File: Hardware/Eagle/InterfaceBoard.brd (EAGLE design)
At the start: 20 parts

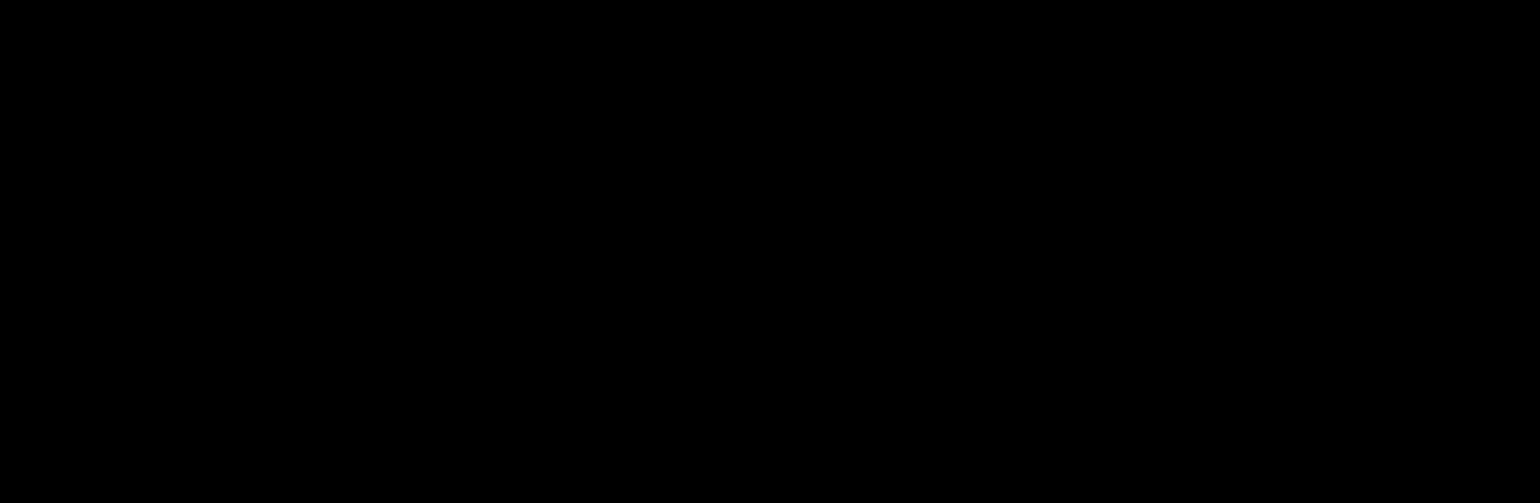
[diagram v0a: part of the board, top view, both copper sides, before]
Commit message: Specified button colors and added Designed by in the PCB layout
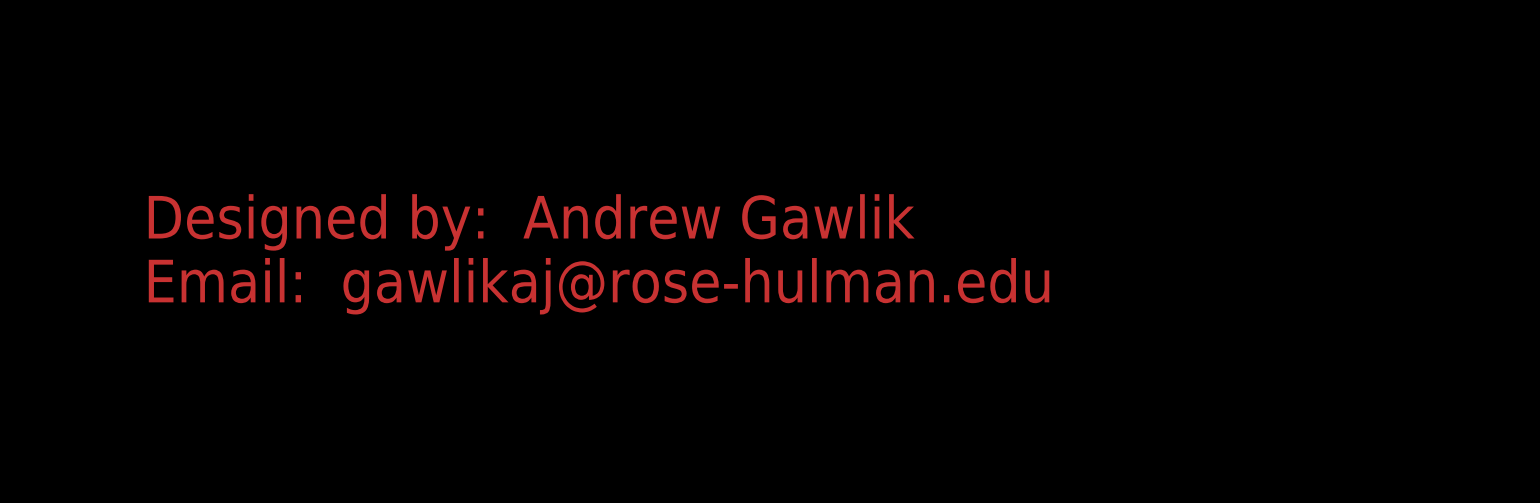
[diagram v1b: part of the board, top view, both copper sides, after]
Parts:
- B0, B9: value (none) -> GREEN
- B1, B6: value (none) -> RED
- B2, B7: value (none) -> BLUE
- B3, B8: value (none) -> YELLOW
- B4, B5: value (none) -> BLACK
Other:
- board text added: "Designed by: Andrew Gawlik Email: gawlikaj@rose-hulman.edu"
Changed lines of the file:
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@@
 <board>
 <plain>
+<text x="88.9" y="-10.16" size="1.778" layer="1">Designed by:  Andrew Gawlik
+Email:  gawlikaj@rose-hulman.edu</text>
 </plain>
 <attributes>
@@
 </autorouter>
 <elements>
-<element name="B9" library="switch-omron" library_urn="urn:adsk.eagle:library:377" package="B3F-10XX" package3d_urn="urn:adsk.eagle:package:27496/1" value="" x="13.335" y="46.99" smashed="yes" rot="R90">
+<element name="B9" library="switch-omron" library_urn="urn:adsk.eagle:library:377" package="B3F-10XX" package3d_urn="urn:adsk.eagle:package:27496/1" value="GREEN" x="13.335" y="46.99" smashed="yes" rot="R90">
 <attribute name="MF" value="" x="13.335" y="46.99" size="1.778" layer="27" rot="R90" display="off"/>
 <attribute name="MPN" value="B3F-1000" x="13.335" y="46.99" size="1.778" layer="27" rot="R90" display="off"/>
@@
 <attribute name="VALUE" x="18.415" y="43.942" size="1.27" layer="27" ratio="10" rot="R90"/>
 </element>
-<element name="B6" library="switch-omron" library_urn="urn:adsk.eagle:library:377" package="B3F-10XX" package3d_urn="urn:adsk.eagle:package:27496/1" value="" x="24.13" y="35.56" smashed="yes" rot="R90">
+<element name="B6" library="switch-omron" library_urn="urn:adsk.eagle:library:377" package="B3F-10XX" package3d_urn="urn:adsk.eagle:package:27496/1" value="RED" x="24.13" y="35.56" smashed="yes" rot="R90">
 <attribute name="MF" value="" x="24.13" y="35.56" size="1.778" layer="27" rot="R90" display="off"/>
 <attribute name="MPN" value="B3F-1000" x="24.13" y="35.56" size="1.778" layer="27" rot="R90" display="off"/>
@@
 <attribute name="VALUE" x="29.21" y="32.512" size="1.27" layer="27" ratio="10" rot="R90"/>
 </element>
-<element name="B7" library="switch-omron" library_urn="urn:adsk.eagle:library:377" package="B3F-10XX" package3d_urn="urn:adsk.eagle:package:27496/1" value="" x="13.335" y="25.4" smashed="yes" rot="R90">
+<element name="B7" library="switch-omron" library_urn="urn:adsk.eagle:library:377" package="B3F-10XX" package3d_urn="urn:adsk.eagle:package:27496/1" value="BLUE" x="13.335" y="25.4" smashed="yes" rot="R90">
 <attribute name="MF" value="" x="13.335" y="25.4" size="1.778" layer="27" rot="R90" display="off"/>
 <attribute name="MPN" value="B3F-1000" x="13.335" y="25.4" size="1.778" layer="27" rot="R90" display="off"/>
@@
 <attribute name="VALUE" x="18.415" y="22.352" size="1.27" layer="27" ratio="10" rot="R90"/>
 </element>
-<element name="B8" library="switch-omron" library_urn="urn:adsk.eagle:library:377" package="B3F-10XX" package3d_urn="urn:adsk.eagle:package:27496/1" value="" x="2.54" y="35.56" smashed="yes" rot="R90">
+<element name="B8" library="switch-omron" library_urn="urn:adsk.eagle:library:377" package="B3F-10XX" package3d_urn="urn:adsk.eagle:package:27496/1" value="YELLOW" x="2.54" y="35.56" smashed="yes" rot="R90">
 <attribute name="MF" value="" x="2.54" y="35.56" size="1.778" layer="27" rot="R90" display="off"/>
 <attribute name="MPN" value="B3F-1000" x="2.54" y="35.56" size="1.778" layer="27" rot="R90" display="off"/>
@@
 <attribute name="VALUE" x="38.9636" y="51.8414" size="0.9906" layer="27" ratio="10" rot="R180"/>
 </element>
-<element name="B2" library="switch-omron" library_urn="urn:adsk.eagle:library:377" package="B3F-10XX" package3d_urn="urn:adsk.eagle:package:27496/1" value="" x="127.635" y="25.4" smashed="yes" rot="R270">
+<element name="B2" library="switch-omron" library_urn="urn:adsk.eagle:library:377" package="B3F-10XX" package3d_urn="urn:adsk.eagle:package:27496/1" value="BLUE" x="127.635" y="25.4" smashed="yes" rot="R270">
 <attribute name="MF" value="" x="127.635" y="25.4" size="1.778" layer="27" rot="R270" display="off"/>
 <attribute name="MPN" value="B3F-1000" x="127.635" y="25.4" size="1.778" layer="27" rot="R270" display="off"/>
@@
 <attribute name="VALUE" x="122.555" y="28.448" size="1.27" layer="27" ratio="10" rot="R270"/>
 </element>
-<element name="B3" library="switch-omron" library_urn="urn:adsk.eagle:library:377" package="B3F-10XX" package3d_urn="urn:adsk.eagle:package:27496/1" value="" x="116.84" y="35.56" smashed="yes" rot="R270">
+<element name="B3" library="switch-omron" library_urn="urn:adsk.eagle:library:377" package="B3F-10XX" package3d_urn="urn:adsk.eagle:package:27496/1" value="YELLOW" x="116.84" y="35.56" smashed="yes" rot="R270">
 <attribute name="MF" value="" x="116.84" y="35.56" size="1.778" layer="27" rot="R270" display="off"/>
 <attribute name="MPN" value="B3F-1000" x="116.84" y="35.56" size="1.778" layer="27" rot="R270" display="off"/>
@@
 <attribute name="VALUE" x="111.76" y="38.608" size="1.27" layer="27" ratio="10" rot="R270"/>
 </element>
-<element name="B0" library="switch-omron" library_urn="urn:adsk.eagle:library:377" package="B3F-10XX" package3d_urn="urn:adsk.eagle:package:27496/1" value="" x="127.635" y="46.99" smashed="yes" rot="R270">
+<element name="B0" library="switch-omron" library_urn="urn:adsk.eagle:library:377" package="B3F-10XX" package3d_urn="urn:adsk.eagle:package:27496/1" value="GREEN" x="127.635" y="46.99" smashed="yes" rot="R270">
 <attribute name="MF" value="" x="127.635" y="46.99" size="1.778" layer="27" rot="R270" display="off"/>
 <attribute name="MPN" value="B3F-1000" x="127.635" y="46.99" size="1.778" layer="27" rot="R270" display="off"/>
@@
 <attribute name="VALUE" x="122.555" y="50.038" size="1.27" layer="27" ratio="10" rot="R270"/>
 </element>
-<element name="B1" library="switch-omron" library_urn="urn:adsk.eagle:library:377" package="B3F-10XX" package3d_urn="urn:adsk.eagle:package:27496/1" value="" x="138.43" y="35.56" smashed="yes" rot="R270">
+<element name="B1" library="switch-omron" library_urn="urn:adsk.eagle:library:377" package="B3F-10XX" package3d_urn="urn:adsk.eagle:package:27496/1" value="RED" x="138.43" y="35.56" smashed="yes" rot="R270">
 <attribute name="MF" value="" x="138.43" y="35.56" size="1.778" layer="27" rot="R270" display="off"/>
 <attribute name="MPN" value="B3F-1000" x="138.43" y="35.56" size="1.778" layer="27" rot="R270" display="off"/>
@@
 <attribute name="VALUE" x="102.0064" y="20.5486" size="0.9906" layer="27" ratio="10"/>
 </element>
-<element name="B5" library="switch-omron" library_urn="urn:adsk.eagle:library:377" package="B3F-10XX" package3d_urn="urn:adsk.eagle:package:27496/1" value="" x="59.69" y="35.56" smashed="yes" rot="R90">
+<element name="B5" library="switch-omron" library_urn="urn:adsk.eagle:library:377" package="B3F-10XX" package3d_urn="urn:adsk.eagle:package:27496/1" value="BLACK" x="59.69" y="35.56" smashed="yes" rot="R90">
 <attribute name="MF" value="" x="46.99" y="25.4" size="1.778" layer="27" rot="R90" display="off"/>
 <attribute name="MPN" value="B3F-1000" x="46.99" y="25.4" size="1.778" layer="27" rot="R90" display="off"/>
@@
 <attribute name="VALUE" x="64.77" y="32.512" size="1.27" layer="27" ratio="10" rot="R90"/>
 </element>
-<element name="B4" library="switch-omron" library_urn="urn:adsk.eagle:library:377" package="B3F-10XX" package3d_urn="urn:adsk.eagle:package:27496/1" value="" x="81.28" y="35.56" smashed="yes" rot="R90">
+<element name="B4" library="switch-omron" library_urn="urn:adsk.eagle:library:377" package="B3F-10XX" package3d_urn="urn:adsk.eagle:package:27496/1" value="BLACK" x="81.28" y="35.56" smashed="yes" rot="R90">
 <attribute name="MF" value="" x="59.69" y="15.24" size="1.778" layer="27" rot="R90" display="off"/>
 <attribute name="MPN" value="B3F-1000" x="59.69" y="15.24" size="1.778" layer="27" rot="R90" display="off"/>
@@
 </drawing>
 <compatibility>
+<note version="6.3" minversion="6.2.2" severity="warning">
+Since Version 6.2.2 text objects can contain more than one line,
+which will not be processed correctly with this version.
+</note>
 <note version="8.2" severity="warning">
 Since Version 8.2, EAGLE supports online libraries. The ids

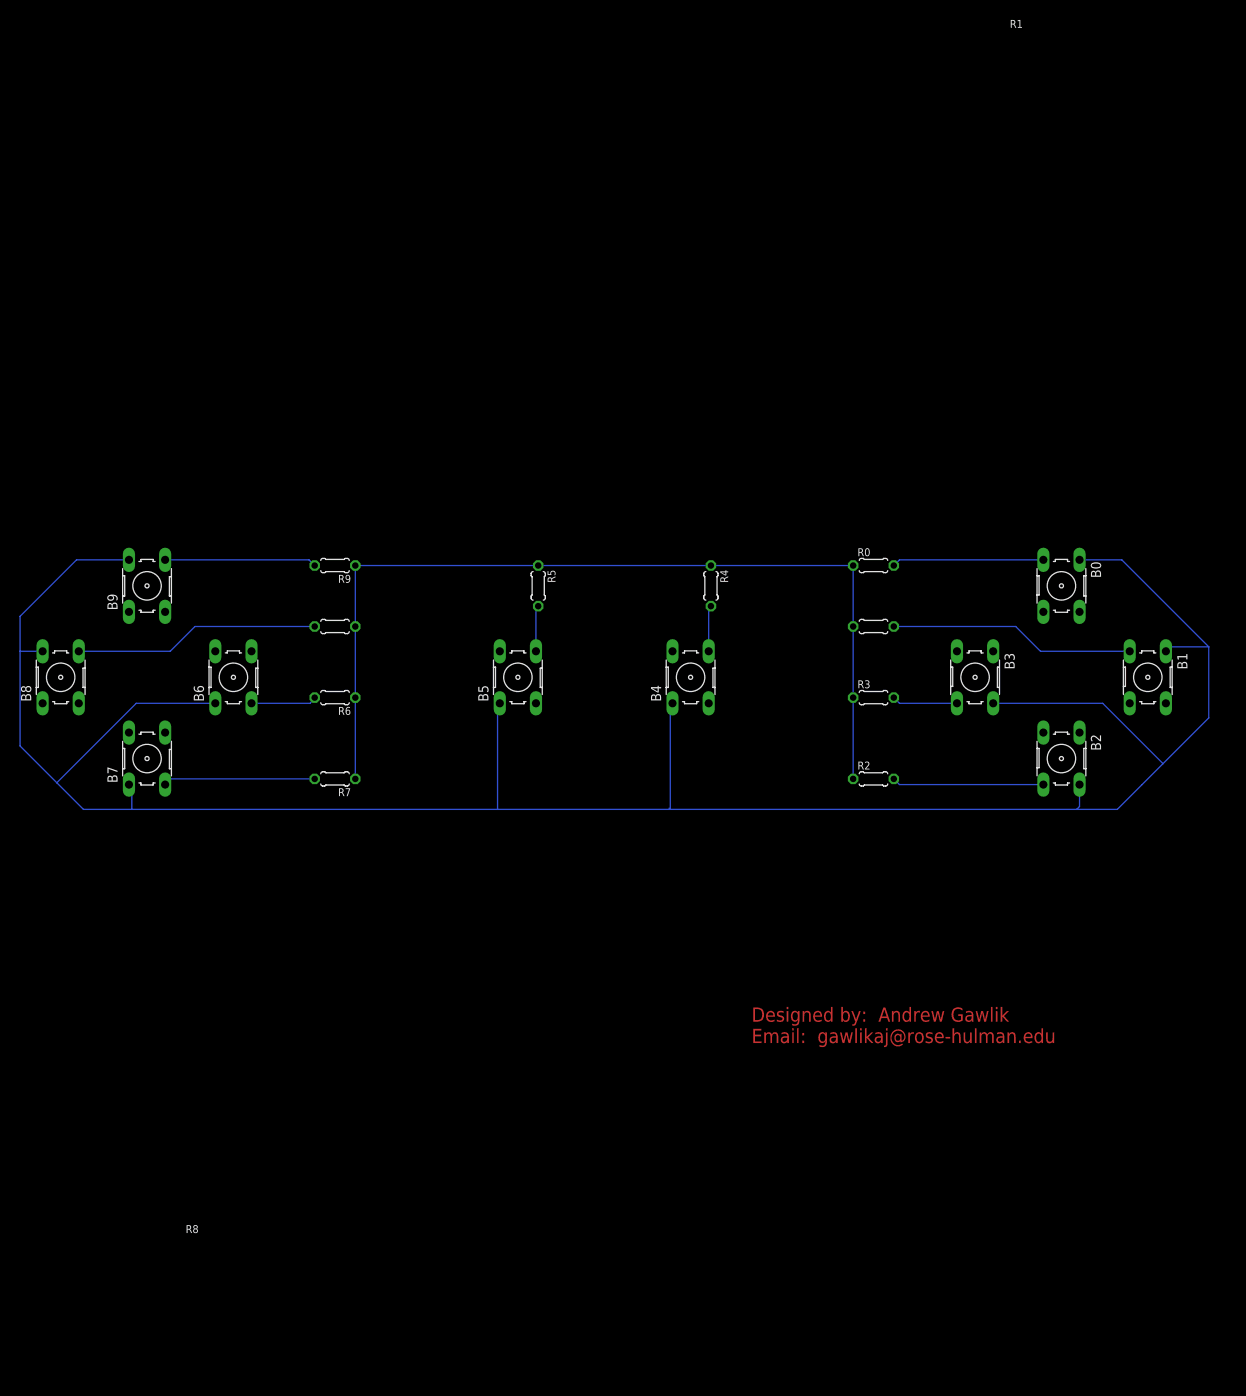
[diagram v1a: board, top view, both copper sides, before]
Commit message: Added speakers to PCB layout
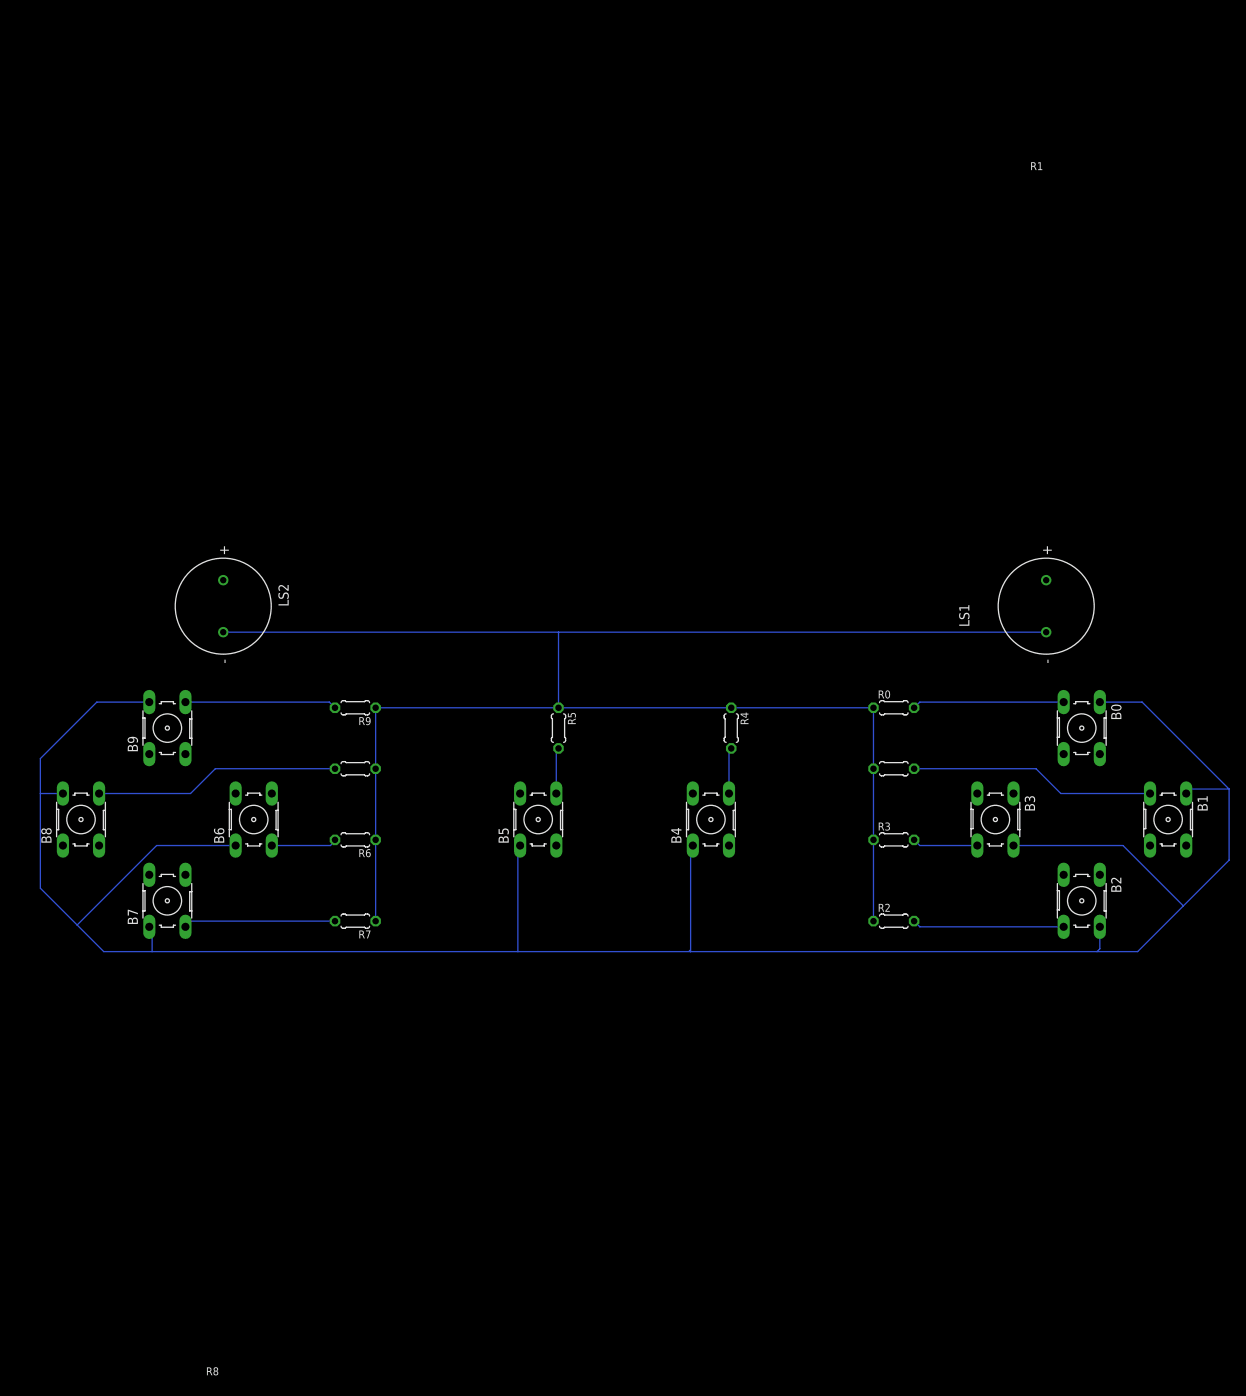
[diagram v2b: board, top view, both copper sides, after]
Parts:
- added LS1, LS2: CEM-1203(42), CEM-1203_42_:CUI_CEM-1203(42)
- moved B0 18.0 mm to (130.2, 29.2)
- moved B5 18.0 mm to (62.2, 17.8)
- moved B6 18.0 mm to (26.7, 17.8)
- moved B8 18.0 mm to (5.08, 17.8)
- moved B9 18.0 mm to (15.9, 29.2)
- moved R0 18.0 mm to (106.7, 31.8)
- moved R2 18.0 mm to (106.7, 5.08)
- moved R3 18.0 mm to (106.7, 15.2)
- moved R4 18.0 mm to (86.4, 29.2)
- moved R5 18.0 mm to (64.8, 29.2)
- moved R6 18.0 mm to (39.4, 15.2)
- moved R7 18.0 mm to (39.4, 5.08)
- moved R9 18.0 mm to (39.4, 31.8)
- moved B1 18.0 mm to (141.0, 17.8)
- moved B2 18.0 mm to (130.2, 7.62)
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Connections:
- net BUTTON0 renamed BTN0
- net BUTTON1 renamed BTN1
- net BUTTON2 renamed BTN2
- net BUTTON3 renamed BTN3
- net BUTTON4 renamed BTN4
- net BUTTON5 renamed BTN5
- net BUTTON6 renamed BTN6
- net BUTTON7 renamed BTN7
- net BUTTON8 renamed BTN8
- net BUTTON9 renamed BTN9
- new net SPK_LEFT: LS2.P
- new net SPK_RIGHT: LS1.P
- net 0: now also LS1.N, LS2.N
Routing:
- net 0: track 115.6 -> 227.9 mm
